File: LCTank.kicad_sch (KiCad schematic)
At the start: 9 parts, among them Q1 2N222A

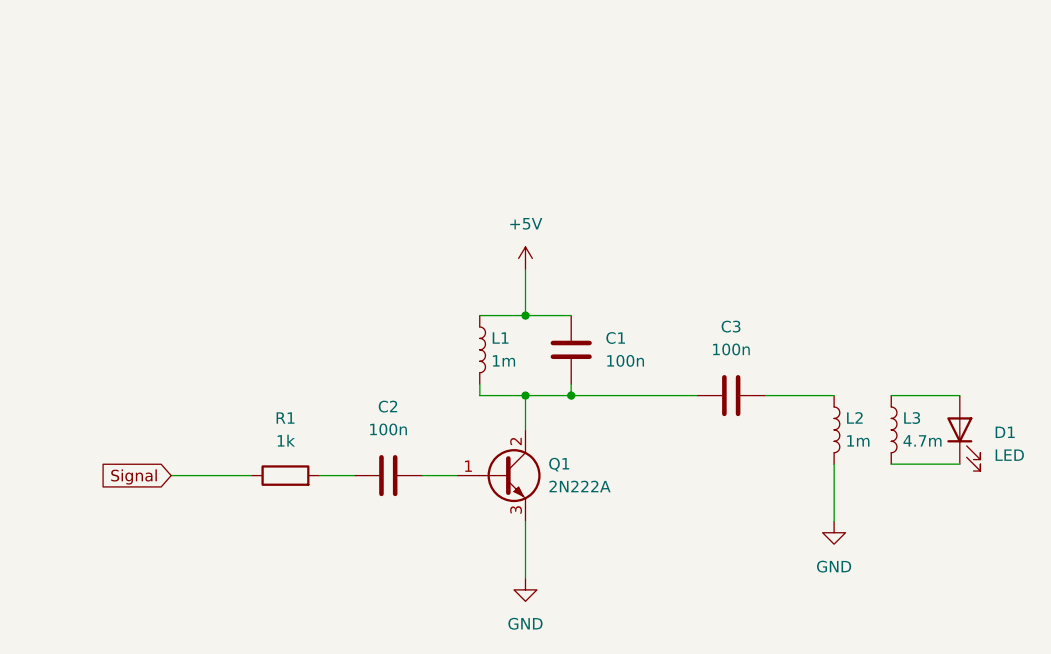
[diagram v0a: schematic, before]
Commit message: Added connectors and pcb
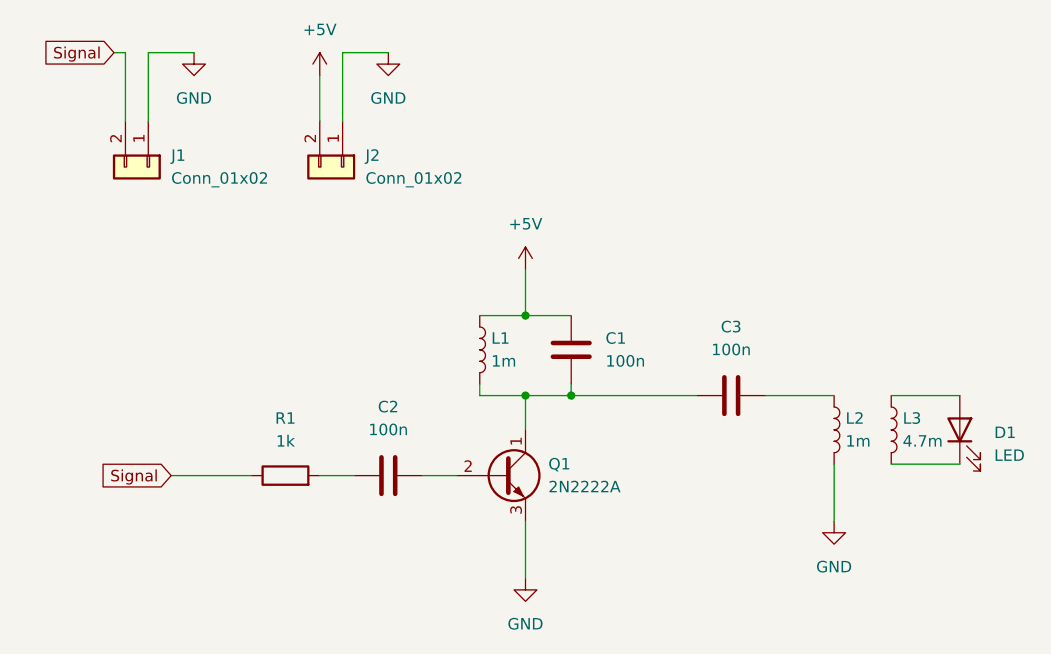
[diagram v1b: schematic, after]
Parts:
- removed Q1: 2N222A, symbol Transistor_BJT:Q_NPN_BCE
- added J1, J2: Conn_01x02, Connector_PinHeader_2.54mm:PinHeader_1x02_P2.54mm_Vertical, symbol Connector_Generic:Conn_01x02
- added Q1: 2N2222A, Package_TO_SOT_THT:TO-92, symbol Transistor_BJT:Q_NPN_CBE
- C1: footprint (none) -> Capacitor_THT:C_Disc_D5.0mm_W2.5mm_P2.50mm
- C2, C3: footprint (none) -> Capacitor_THT:C_Disc_D5.1mm_W3.2mm_P5.00mm
- D1: footprint (none) -> LED_THT:LED_D5.0mm
- L1, L2, L3: footprint (none) -> Inductor_THT:L_Axial_L6.6mm_D2.7mm_P10.16mm_Horizontal_Vishay_IM-2
- R1: footprint (none) -> Resistor_THT:R_Axial_DIN0207_L6.3mm_D2.5mm_P7.62mm_Horizontal
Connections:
- net +5V: now also J2.2 (Pin_2)
- net GND: now also J1.1 (Pin_1), J2.1 (Pin_1), Q1.3 (E)
- net Signal: now also J1.2 (Pin_2)
- net at C2.2: now also Q1.2 (B)
- net at C1.2, C3.1, L1.2: now also Q1.1 (C)
